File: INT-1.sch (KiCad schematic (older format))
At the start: 53 parts

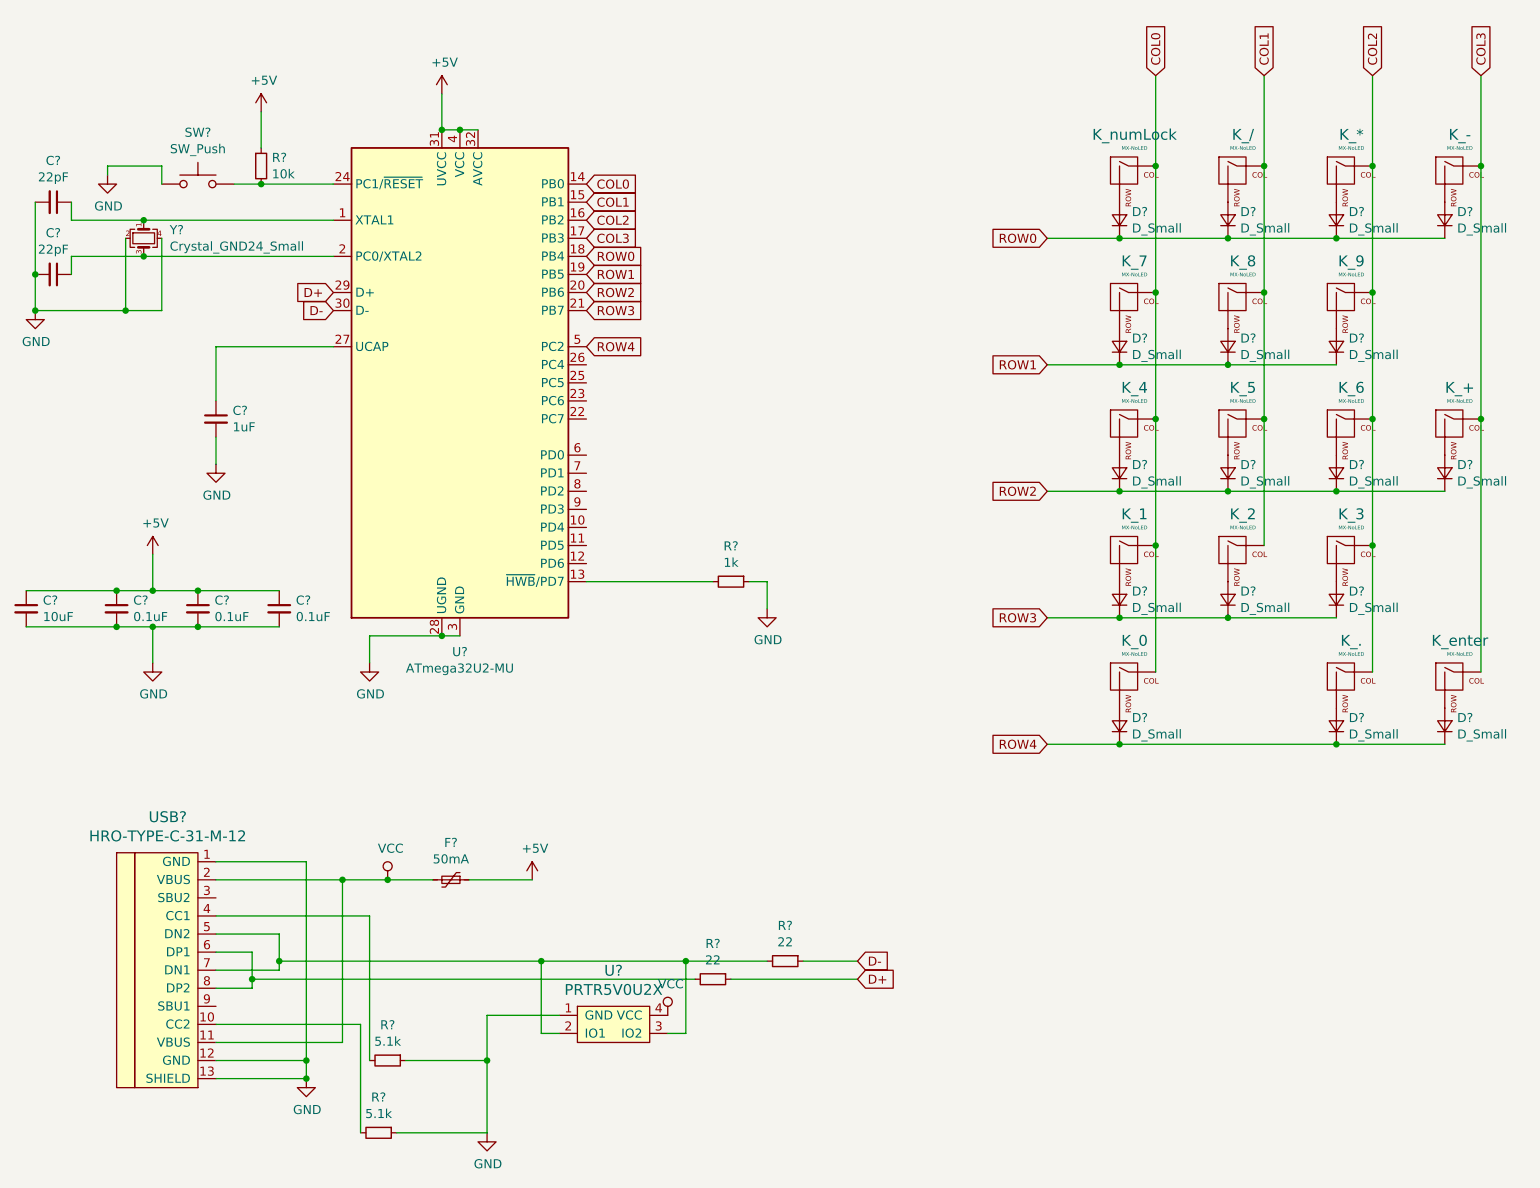
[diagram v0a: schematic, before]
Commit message: Assigned Footprints
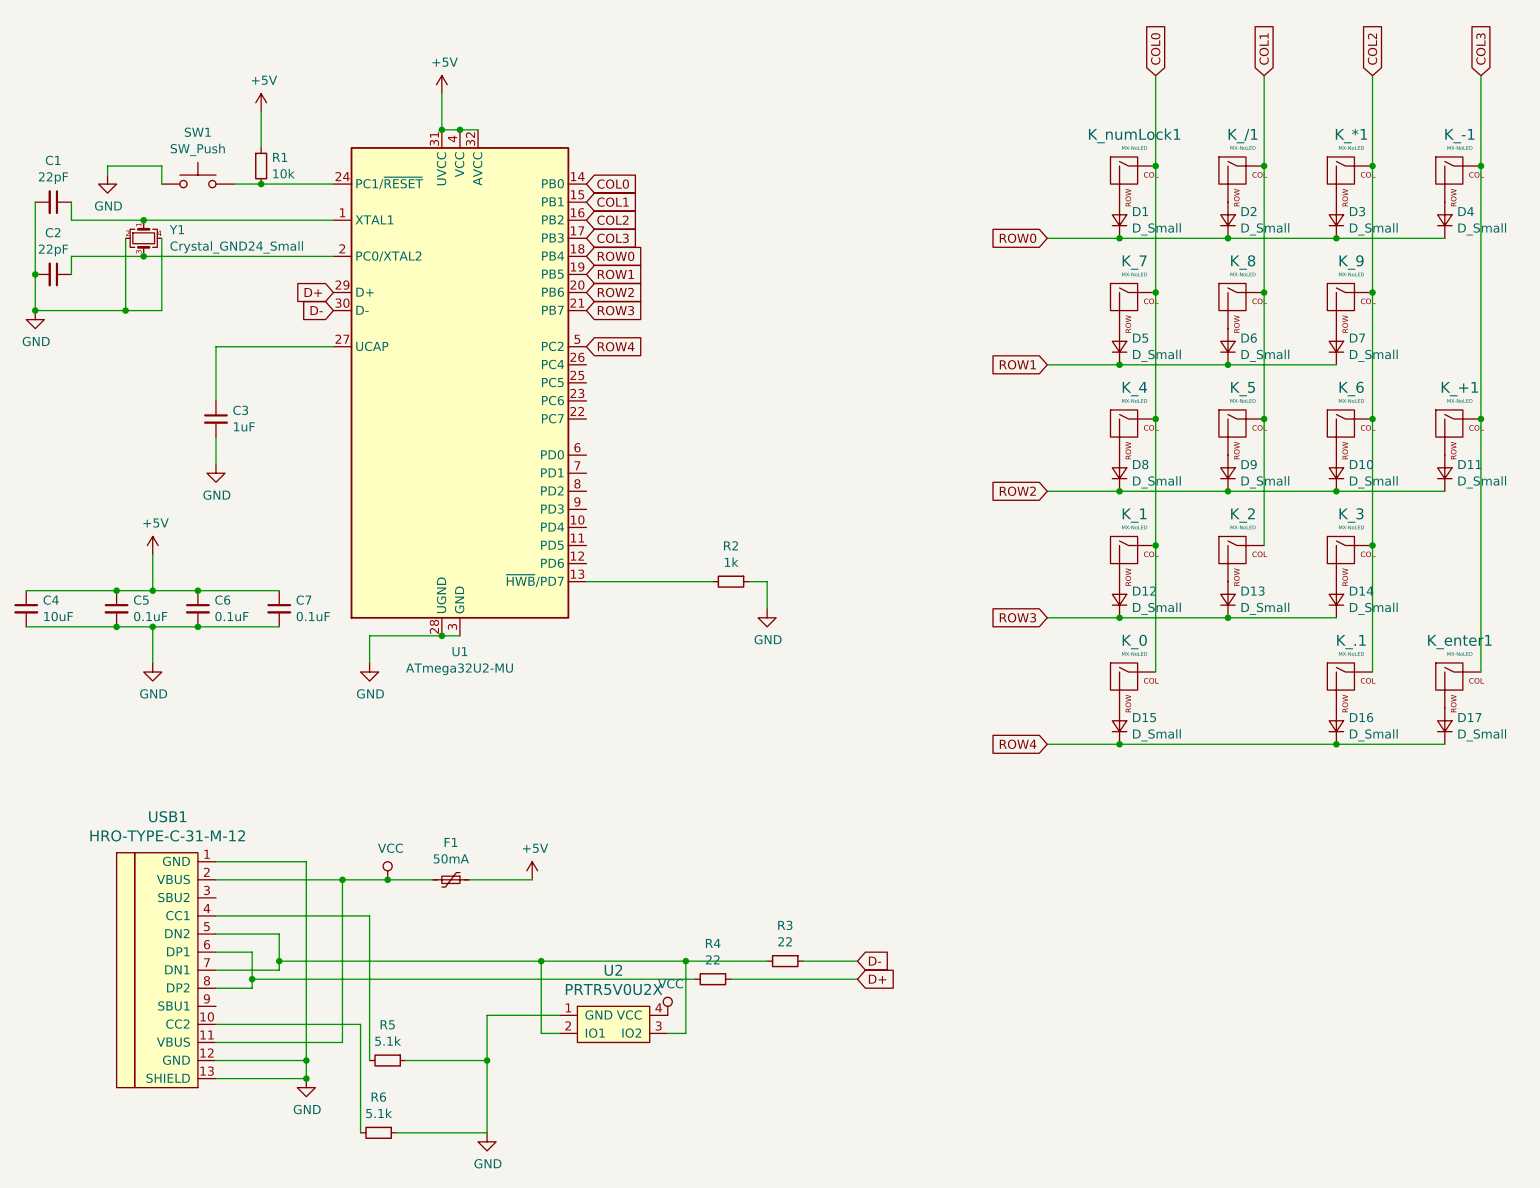
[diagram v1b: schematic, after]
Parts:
- C1, C2, C3, C4, C5, C6, C7: renamed from C?; footprint (none) -> Capacitor_SMD:C_0603_1608Metric
- D1, D10, D11, D12, D13, D14, D15, D16, D17, D2, D3, D4, D5, D6, D7, D8, D9: renamed from D?; footprint (none) -> Diode_SMD:D_SOD-123
- F1: renamed from F?; footprint (none) -> Fuse:Fuse_1206_3216Metric
- K_*1: renamed from K_*; footprint (none) -> MX_Only:MXOnly-1U-Hotswap
- K_+1: renamed from K_+; footprint (none) -> MX_2U_Hotswap_Vertical:MX-2U-Hotswap-Vertical
- K_-1: renamed from K_-; footprint (none) -> MX_Only:MXOnly-1U
- K_.1: renamed from K_.; footprint (none) -> MX_Only:MXOnly-1U-Hotswap
- K_/1: renamed from K_/; footprint (none) -> MX_Only:MXOnly-1U
- K_0: footprint (none) -> MX_Only:MXOnly-2U-Hotswap
- K_1, K_2, K_3, K_4, K_5, K_6, K_7, K_8, K_9: footprint (none) -> MX_Only:MXOnly-1U-Hotswap
- K_enter1: renamed from K_enter; footprint (none) -> MX_2U_Hotswap_Vertical:MX-2U-Hotswap-Vertical
- K_numLock1: renamed from K_numLock; footprint (none) -> MX_Only:MXOnly-1U
- R1, R2, R3, R4, R5, R6: renamed from R?; footprint (none) -> Resistor_SMD:R_0805_2012Metric
- SW1: renamed from SW?; footprint (none) -> random-keyboard-parts:SKQG-1155865
- U2: renamed from U?; footprint (none) -> random-keyboard-parts:SOT143B
- USB1: renamed from USB?; footprint (none) -> Type-C:HRO-TYPE-C-31-M-12
- Y1: renamed from Y?; footprint (none) -> Crystal:Crystal_SMD_3225-4Pin_3.2x2.5mm
- gave numbers to parts that had none: 1

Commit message: Finished diode placement
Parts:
- K_-1, K_/1, K_numLock1: footprint MX_Only:MXOnly-1U -> MX_Only:MXOnly-1U-Hotswap
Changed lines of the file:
@@
 F 0 "K_numLock1" H 6733 2173 60  0000 C CNN
 F 1 "MX-NoLED" H 6733 2099 20  0000 C CNN
-F 2 "MX_Only:MXOnly-1U" H 6075 1925 60  0001 C CNN
+F 2 "MX_Only:MXOnly-1U-Hotswap" H 6075 1925 60  0001 C CNN
 F 3 "" H 6075 1925 60  0001 C CNN
 	1    6700 1950
@@
 F 0 "K_/1" H 7333 2173 60  0000 C CNN
 F 1 "MX-NoLED" H 7333 2099 20  0000 C CNN
-F 2 "MX_Only:MXOnly-1U" H 6675 1925 60  0001 C CNN
+F 2 "MX_Only:MXOnly-1U-Hotswap" H 6675 1925 60  0001 C CNN
 F 3 "" H 6675 1925 60  0001 C CNN
 	1    7300 1950
@@
 F 0 "K_-1" H 8533 2173 60  0000 C CNN
 F 1 "MX-NoLED" H 8533 2099 20  0000 C CNN
-F 2 "MX_Only:MXOnly-1U" H 7875 1925 60  0001 C CNN
+F 2 "MX_Only:MXOnly-1U-Hotswap" H 7875 1925 60  0001 C CNN
 F 3 "" H 7875 1925 60  0001 C CNN
 	1    8500 1950

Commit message: Finished trace routing
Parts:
- removed C7: 0.1uF, Capacitor_SMD:C_0603_1608Metric, symbol Device:C_Small
- C4: value 10uF -> 4.7uF
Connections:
- net COL0: now also U1.21 (PB7); no longer U1.14 (PB0)
- net COL1: now also U1.20 (PB6); no longer U1.15 (PB1)
- net COL2: now also U1.19 (PB5); no longer U1.16 (PB2)
- net COL3: now also U1.15 (PB1); no longer U1.17 (PB3)
- net ROW0: now also U1.16 (PB2); no longer U1.18 (PB4)
- net ROW1: now also U1.17 (PB3); no longer U1.19 (PB5)
- net ROW2: now also U1.18 (PB4); no longer U1.20 (PB6)
- net ROW3: now also U1.22 (PC7); no longer U1.21 (PB7)
- net ROW4: now also U1.23 (PC6); no longer U1.5 (PC2)
- net at R3.2, U2.3 (IO2), USB1.5 (DN2)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: no longer U2.2 (IO1)
- net at R4.2, USB1.6 (DP1), USB1.8 (DP2): now also U2.2 (IO1)
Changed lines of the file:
@@
 P 600 4350
 F 0 "C4" H 692 4396 50  0000 L CNN
-F 1 "10uF" H 692 4305 50  0000 L CNN
+F 1 "4.7uF" H 692 4305 50  0000 L CNN
 F 2 "Capacitor_SMD:C_0603_1608Metric" H 600 4350 50  0001 C CNN
 F 3 "~" H 600 4350 50  0001 C CNN
@@
 	1    0    0    -1
 $EndComp
-$Comp
-L Device:C_Small C7
-U 1 1 62050A82
-P 2000 4350
-F 0 "C7" H 2092 4396 50  0000 L CNN
-F 1 "0.1uF" H 2092 4305 50  0000 L CNN
-F 2 "Capacitor_SMD:C_0603_1608Metric" H 2000 4350 50  0001 C CNN
-F 3 "~" H 2000 4350 50  0001 C CNN
-	1    2000 4350
-	1    0    0    -1
-$EndComp
-Wire Wire Line
-	2000 4250 1550 4250
 Connection ~ 1100 4250
 Wire Wire Line
 	1100 4250 600  4250
-Connection ~ 1550 4250
-Wire Wire Line
-	1550 4250 1300 4250
 Wire Wire Line
 	600  4450 1100 4450
 Connection ~ 1100 4450
 Wire Wire Line
-	1100 4450 1300 4450
-Connection ~ 1550 4450
-Wire Wire Line
-	1550 4450 2000 4450
-Wire Wire Line
-	1300 4250 1300 4050
-Connection ~ 1300 4250
-Wire Wire Line
-	1300 4250 1100 4250
+	1100 4250 1100 4050
 $Comp
 L power:+5V #PWR0108
 U 1 1 62052A7B
-P 1300 4050
-F 0 "#PWR0108" H 1300 3900 50  0001 C CNN
-F 1 "+5V" H 1315 4223 50  0000 C CNN
-F 2 "" H 1300 4050 50  0001 C CNN
-F 3 "" H 1300 4050 50  0001 C CNN
-	1    1300 4050
-	1    0    0    -1
-$EndComp
-Wire Wire Line
-	1300 4450 1300 4650
-Connection ~ 1300 4450
-Wire Wire Line
-	1300 4450 1550 4450
+P 1100 4050
+F 0 "#PWR0108" H 1100 3900 50  0001 C CNN
+F 1 "+5V" H 1115 4223 50  0000 C CNN
+F 2 "" H 1100 4050 50  0001 C CNN
+F 3 "" H 1100 4050 50  0001 C CNN
+	1    1100 4050
+	1    0    0    -1
+$EndComp
+Wire Wire Line
+	1100 4450 1100 4650
 $Comp
 L power:GND #PWR0109
 U 1 1 6205416B
-P 1300 4650
-F 0 "#PWR0109" H 1300 4400 50  0001 C CNN
-F 1 "GND" H 1305 4477 50  0000 C CNN
-F 2 "" H 1300 4650 50  0001 C CNN
-F 3 "" H 1300 4650 50  0001 C CNN
-	1    1300 4650
+P 1100 4650
+F 0 "#PWR0109" H 1100 4400 50  0001 C CNN
+F 1 "GND" H 1105 4477 50  0000 C CNN
+F 2 "" H 1100 4650 50  0001 C CNN
+F 3 "" H 1100 4650 50  0001 C CNN
+	1    1100 4650
 	1    0    0    -1
 $EndComp
@@
 	3550 6700 3450 6700
 Wire Wire Line
-	3450 6700 3450 6300
-Connection ~ 3450 6300
-Wire Wire Line
-	3450 6300 4250 6300
-Wire Wire Line
 	2000 6150 2000 6300
-Wire Wire Line
-	2000 6300 3450 6300
 Connection ~ 2000 6300
 Wire Wire Line
 	2000 6300 2000 6350
 Wire Wire Line
-	1850 6400 4300 6400
+	1850 6400 3450 6400
 Wire Wire Line
 	1850 6250 1850 6400
@@
 Text GLabel 6250 2300 0    50   Input ~ 0
 ROW0
-Text GLabel 3700 2000 2    50   Input ~ 0
+Text GLabel 3700 2700 2    50   Input ~ 0
 COL0
+Text GLabel 3700 2600 2    50   Input ~ 0
+COL1
+Text GLabel 3700 2500 2    50   Input ~ 0
+COL2
 Text GLabel 3700 2100 2    50   Input ~ 0
-COL1
+COL3
 Text GLabel 3700 2200 2    50   Input ~ 0
-COL2
+ROW0
 Text GLabel 3700 2300 2    50   Input ~ 0
-COL3
+ROW1
 Text GLabel 3700 2400 2    50   Input ~ 0
-ROW0
-Text GLabel 3700 2500 2    50   Input ~ 0
-ROW1
-Text GLabel 3700 2600 2    50   Input ~ 0
 ROW2
-Text GLabel 3700 2700 2    50   Input ~ 0
+Text GLabel 3700 3300 2    50   Input ~ 0
 ROW3
-Text GLabel 3700 2900 2    50   Input ~ 0
+Text GLabel 3700 3200 2    50   Input ~ 0
 ROW4
+Wire Wire Line
+	1100 4250 1550 4250
+Wire Wire Line
+	1100 4450 1550 4450
+Wire Wire Line
+	2000 6300 4250 6300
+Wire Wire Line
+	3450 6700 3450 6400
+Connection ~ 3450 6400
+Wire Wire Line
+	3450 6400 4300 6400
 $EndSCHEMATC
